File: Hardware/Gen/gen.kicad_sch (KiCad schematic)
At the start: 43 parts, among them J1 Screw_Terminal_01x03, J2 XLR4, J3 XLR3, U1 TPS56339DDCT, U3 TPS560430YDBVR

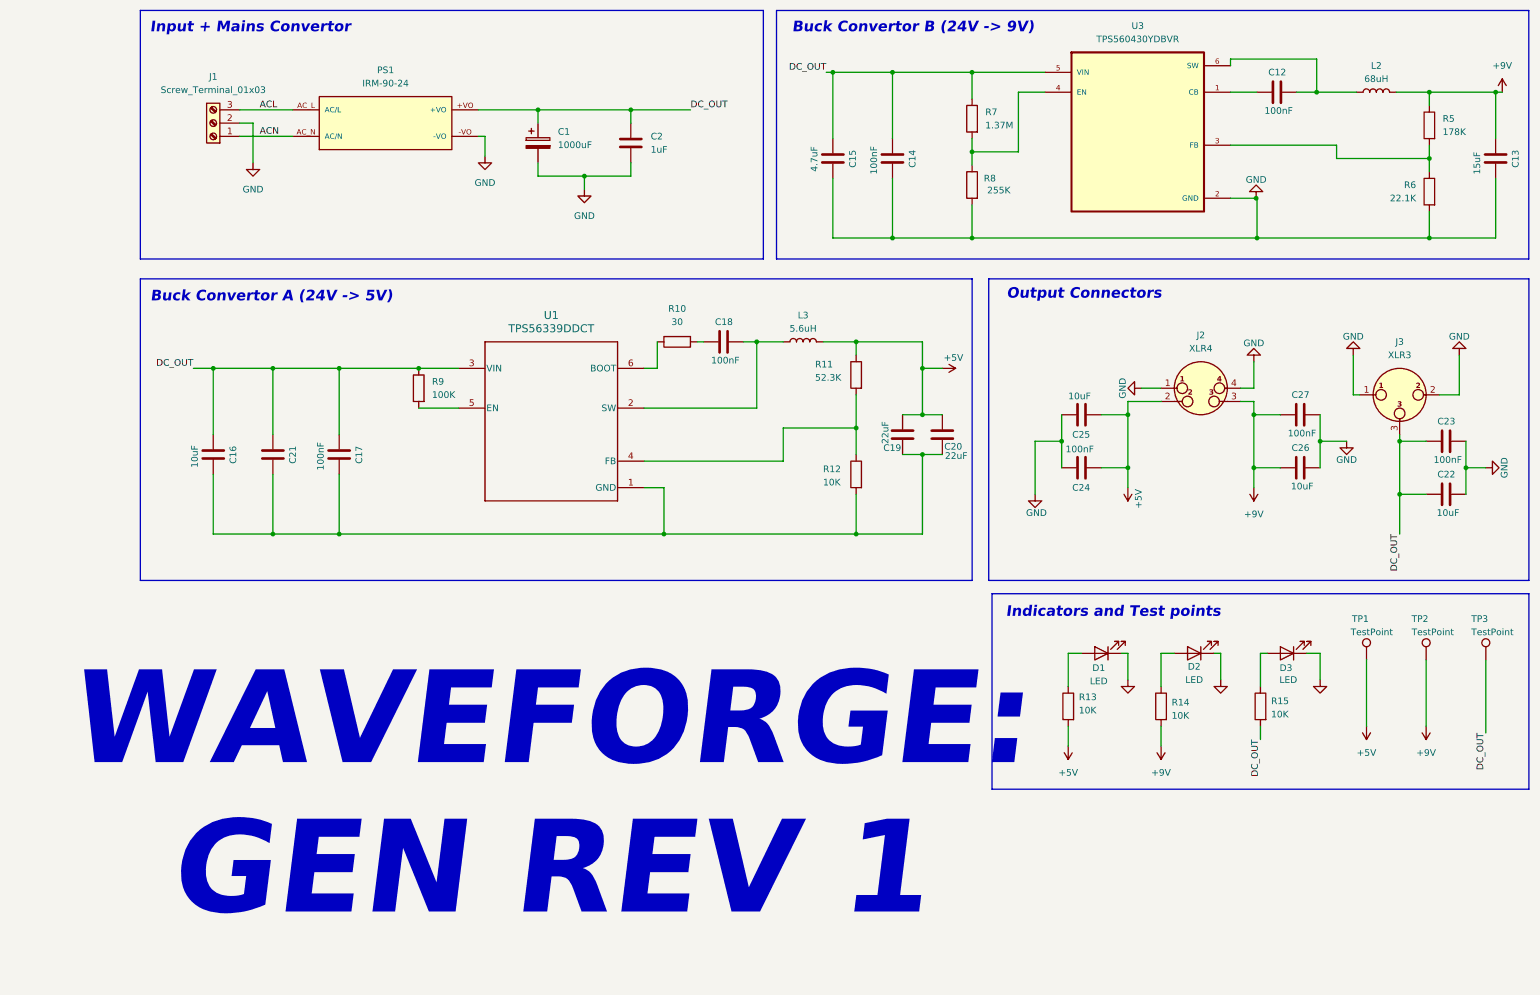
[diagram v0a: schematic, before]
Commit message: Gen: Rev 1 schem done, footprints assignment underway
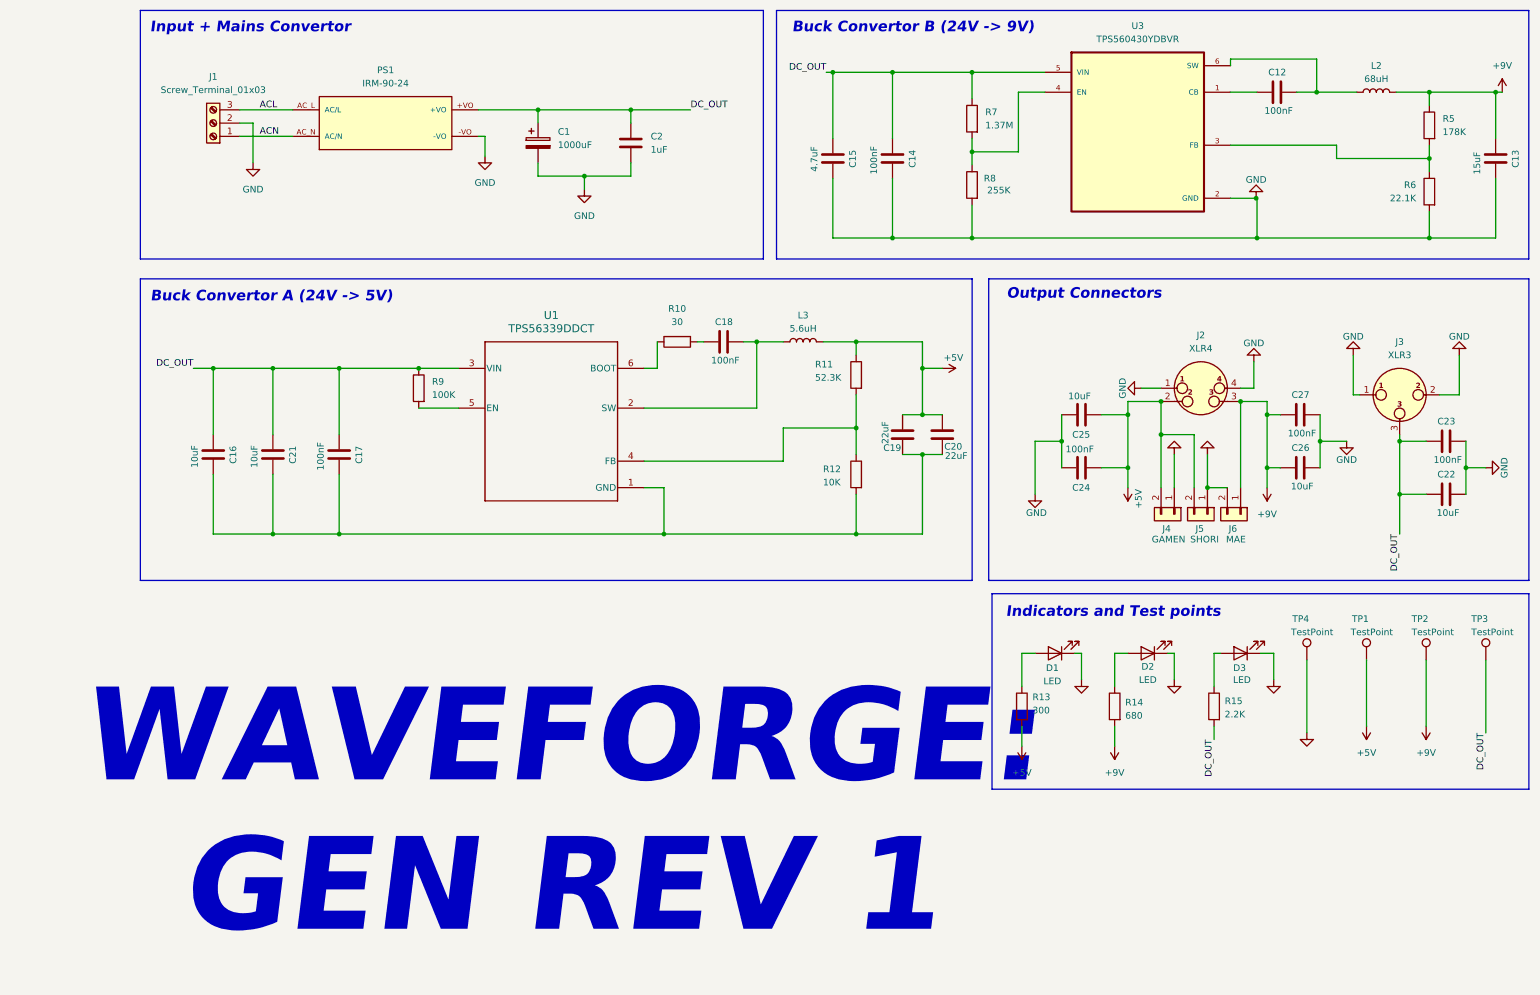
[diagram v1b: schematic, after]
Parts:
- added J4: GAMEN, Connector_JST:JST_XH_S2B-XH-A_1x02_P2.50mm_Horizontal, symbol Connector_Generic:Conn_01x02
- added J5: SHORI, Connector_JST:JST_XH_S2B-XH-A_1x02_P2.50mm_Horizontal, symbol Connector_Generic:Conn_01x02
- added J6: MAE, Connector_JST:JST_PH_S2B-PH-K_1x02_P2.00mm_Horizontal, symbol Connector_Generic:Conn_01x02
- added TP4: TestPoint, symbol Connector:TestPoint
- C12, C14, C17, C18, C23, C24, C27: footprint Capacitor_THT:C_Disc_D5.0mm_W2.5mm_P2.50mm -> Capacitor_SMD:C_0402_1005Metric_Pad0.74x0.62mm_HandSolder
- C13, C15, C16, C19, C20, C21, C22, C25, C26: footprint Capacitor_THT:C_Disc_D5.0mm_W2.5mm_P2.50mm -> Capacitor_SMD:C_0603_1608Metric_Pad1.08x0.95mm_HandSolder
- D1, D2, D3: footprint (none) -> LED_SMD:LED_0805_2012Metric
- L2: footprint (none) -> My footprints:WE-LQS_2512
- L3: footprint (none) -> My footprints:WE-XHMI_4040
- R13: value 10K -> 300
- R14: value 10K -> 680
- R15: value 10K -> 2.2K
- U1: footprint DDC0006A_N -> (none)
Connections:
- net +5V: now also J4.2 (Pin_2), J5.2 (Pin_2)
- net +9V: now also J6.1 (Pin_1)
- net GND: now also J4.1 (Pin_1), J5.1 (Pin_1), J6.2 (Pin_2), TP4.1
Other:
- moved on the sheet: D1, D2, D3, R13, R14, R15

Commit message: Gen: Layout rev 1 done and routing started
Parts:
- added H1, H2, H3: MountingHole, MountingHole:MountingHole_4mm, symbol Mechanical:MountingHole
- J2: footprint (none) -> TerminalBlock_CUI:TerminalBlock_CUI_TB007-508-04_1x04_P5.08mm_Horizontal
- J3: footprint (none) -> TerminalBlock_CUI:TerminalBlock_CUI_TB007-508-03_1x03_P5.08mm_Horizontal
- R10, R12, R13, R14: footprint (none) -> Resistor_SMD:R_0402_1005Metric_Pad0.72x0.64mm_HandSolder
- R11, R5, R6, R7, R8, R9: footprint (none) -> Resistor_SMD:R_0603_1608Metric_Pad0.98x0.95mm_HandSolder
- R15: footprint (none) -> Resistor_SMD:R_0805_2012Metric_Pad1.20x1.40mm_HandSolder
- TP1, TP2, TP3, TP4: footprint (none) -> TestPoint:TestPoint_Pad_D2.5mm
- U1: footprint (none) -> Package_TO_SOT_SMD:SOT-23-6_Handsoldering
- U3: footprint TPS560430YDBVR:SOT95P280X145-6N -> Package_TO_SOT_SMD:SOT-23-6_Handsoldering
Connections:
- net +5V: now also J2.3; no longer J2.2
- net +9V: now also J2.1; no longer J2.3
- net DC_OUT: now also J3.1; no longer J3.3
- net GND: now also C16.1, C17.1, C19.1, C20.1, C21.1, J2.2, J3.3, R12.2, U1.1 (GND); no longer J2.1, J3.1
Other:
- moved on the sheet: J3

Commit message: Gen: Layout and routing complete rev 1
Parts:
- C23: footprint Capacitor_SMD:C_0402_1005Metric_Pad0.74x0.62mm_HandSolder -> Capacitor_SMD:C_0603_1608Metric_Pad1.08x0.95mm_HandSolder
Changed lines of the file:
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@@
 			)
 		)
-		(property "Footprint" "Capacitor_SMD:C_0402_1005Metric_Pad0.74x0.62mm_HandSolder"
+		(property "Footprint" "Capacitor_SMD:C_0603_1608Metric_Pad1.08x0.95mm_HandSolder"
 			(at 260.35 95.5548 0)
 			(hide yes)

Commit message: Gen: New Routing, More memes and better buck layouts (rev 2)
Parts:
- added J7: Screw_Terminal_01x02, TerminalBlock_CUI:TerminalBlock_CUI_TB007-508-02_1x02_P5.08mm_Horizontal, symbol Connector:Screw_Terminal_01x02
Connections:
- net GND: now also J7.1 (Pin_1); no longer J1.2 (Pin_2)
- no-connect marks 0 -> 2
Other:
- note added: "Buck Convertor A (24V -> 5V @2A)"
- note removed: "Buck Convertor A (24V -> 5V)"
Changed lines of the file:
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@@
 		)
 	)
-	(text "Buck Convertor A (24V -> 5V)"
+	(text "Buck Convertor A (24V -> 5V @2A)"
 		(exclude_from_sim no)
-		(at 39.116 68.834 0)
+		(at 44.196 68.326 0)
 		(effects
 			(font
@@
 		(color 0 0 0 0)
 	)
+	(no_connect
+		(at 33.02 35.56)
+	)
+	(no_connect
+		(at 33.02 48.26)
+	)
 	(wire
 		(pts
@@
 	(wire
 		(pts
-			(xy 35.56 35.56) (xy 33.02 35.56)
-		)
-		(stroke
-			(width 0)
-			(type default)
-		)
-	)
-	(wire
-		(pts
 			(xy 158.0915 46.1478) (xy 158.0915 57.5778)
 		)
@@
 	(wire
 		(pts
-			(xy 35.56 43.18) (xy 35.56 35.56)
-		)
-		(stroke
-			(width 0)
-			(type default)
-		)
-	)
-	(wire
-		(pts
 			(xy 52.07 114.3) (xy 92.71 114.3)
 		)
@@
 	(wire
 		(pts
+			(xy 33.02 50.8) (xy 36.83 50.8)
+		)
+		(stroke
+			(width 0)
+			(type default)
+		)
+	)
+	(wire
+		(pts
 			(xy 229.87 86.36) (xy 229.87 91.44)
 		)
@@
 	)
 	(symbol
+		(lib_id "Connector:Screw_Terminal_01x02")
+		(at 27.94 50.8 180)
+		(unit 1)
+		(body_style 1)
+		(exclude_from_sim no)
+		(in_bom yes)
+		(on_board yes)
+		(in_pos_files yes)
+		(dnp no)
+		(fields_autoplaced yes)
+		(property "Reference" "J7"
+			(at 27.94 41.91 0)
+			(show_name no)
+			(do_not_autoplace no)
+			(effects
+				(font
+					(size 1.27 1.27)
+				)
+			)
+		)
+		(property "Value" "Screw_Terminal_01x02"
+			(at 27.94 44.45 0)
+			(show_name no)
+			(do_not_autoplace no)
+			(effects
+				(font
+					(size 1.27 1.27)
+				)
+			)
+		)
+		(property "Footprint" "TerminalBlock_CUI:TerminalBlock_CUI_TB007-508-02_1x02_P5.08mm_Horizontal"
+			(at 27.94 50.8 0)
+			(hide yes)
+			(show_name no)
+			(do_not_autoplace no)
+			(effects
+				(font
+					(size 1.27 1.27)
+				)
+			)
+		)
+		(property "Datasheet" ""
+			(at 27.94 50.8 0)
+			(hide yes)
+			(show_name no)
+			(do_not_autoplace no)
+			(effects
+				(font
+					(size 1.27 1.27)
+				)
+			)
+		)
+		(property "Description" "Generic screw terminal, single row, 01x02, script generated (kicad-library-utils/schlib/autogen/connector/)"
+			(at 27.94 50.8 0)
+			(hide yes)
+			(show_name no)
+			(do_not_autoplace no)
+			(effects
+				(font
+					(size 1.27 1.27)
+				)
+			)
+		)
+		(pin "1"
+		)
+		(pin "2"
+		)
+		(instances
+			(project "gen"
+				(path "/012cfd84-d095-43cc-b661-50b6ce25f7db"
+					(reference "J7")
+					(unit 1)
+				)
+			)
+		)
+	)
+	(symbol
 		(lib_id "power:GND")
 		(at 205.74 86.36 270)
@@
 	)
 	(symbol
+		(lib_id "power:GND")
+		(at 36.83 50.8 90)
+		(unit 1)
+		(body_style 1)
+		(exclude_from_sim no)
+		(in_bom yes)
+		(on_board yes)
+		(in_pos_files yes)
+		(dnp no)
+		(fields_autoplaced yes)
+		(property "Reference" "#PWR027"
+			(at 43.18 50.8 0)
+			(hide yes)
+			(show_name no)
+			(do_not_autoplace no)
+			(effects
+				(font
+					(size 1.27 1.27)
+				)
+			)
+		)
+		(property "Value" "GND"
+			(at 40.64 50.7999 90)
+			(show_name no)
+			(do_not_autoplace no)
+			(effects
+				(font
+					(size 1.27 1.27)
+				)
+				(justify right)
+			)
+		)
+		(property "Footprint" ""
+			(at 36.83 50.8 0)
+			(hide yes)
+			(show_name no)
+			(do_not_autoplace no)
+			(effects
+				(font
+					(size 1.27 1.27)
+				)
+			)
+		)
+		(property "Datasheet" ""
+			(at 36.83 50.8 0)
+			(hide yes)
+			(show_name no)
+			(do_not_autoplace no)
+			(effects
+				(font
+					(size 1.27 1.27)
+				)
+			)
+		)
+		(property "Description" "Power symbol creates a global label with name \"GND\" , ground"
+			(at 36.83 50.8 0)
+			(hide yes)
+			(show_name no)
+			(do_not_autoplace no)
+			(effects
+				(font
+					(size 1.27 1.27)
+				)
+			)
+		)
+		(pin "1"
+		)
+		(instances
+			(project "gen"
+				(path "/012cfd84-d095-43cc-b661-50b6ce25f7db"
+					(reference "#PWR027")
+					(unit 1)
+				)
+			)
+		)
+	)
+	(symbol
 		(lib_id "Device:C")
 		(at 39.37 99.06 0)
@@
 					(unit 1)
 				)
-			)
-		)
-	)
-	(symbol
-		(lib_id "power:GND")
-		(at 35.56 43.18 0)
-		(unit 1)
-		(body_style 1)
-		(exclude_from_sim no)
-		(in_bom yes)
-		(on_board yes)
-		(in_pos_files yes)
-		(dnp no)
-		(fields_autoplaced yes)
-		(property "Reference" "#PWR01"
-			(at 35.56 49.53 0)
-			(hide yes)
-			(show_name no)
-			(do_not_autoplace no)
-			(effects
-				(font
-					(size 1.27 1.27)
-				)
-			)
-		)
-		(property "Value" "GND"
-			(at 35.56 48.26 0)
-			(show_name no)
-			(do_not_autoplace no)
-			(effects
-				(font
-					(size 1.27 1.27)
-				)
-			)
-		)
-		(property "Footprint" ""
-			(at 35.56 43.18 0)
-			(hide yes)
-			(show_name no)
-			(do_not_autoplace no)
-			(effects
-				(font
-					(size 1.27 1.27)
-				)
-			)
-		)
-		(property "Datasheet" ""
-			(at 35.56 43.18 0)
-			(hide yes)
-			(show_name no)
-			(do_not_autoplace no)
-			(effects
-				(font
-					(size 1.27 1.27)
-				)
-			)
-		)
-		(property "Description" "Power symbol creates a global label with name \"GND\" , ground"
-			(at 35.56 43.18 0)
-			(hide yes)
-			(show_name no)
-			(do_not_autoplace no)
-			(effects
-				(font
-					(size 1.27 1.27)
-				)
-			)
-		)
-		(pin "1"
-		)
-		(instances
-			(project "gen"
-				(path "/012cfd84-d095-43cc-b661-50b6ce25f7db"
-					(reference "#PWR01")
-					(unit 1)
-				)
